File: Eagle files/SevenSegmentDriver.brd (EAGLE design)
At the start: 100 x 80 mm, 12 parts, among them IC1 74HC595D

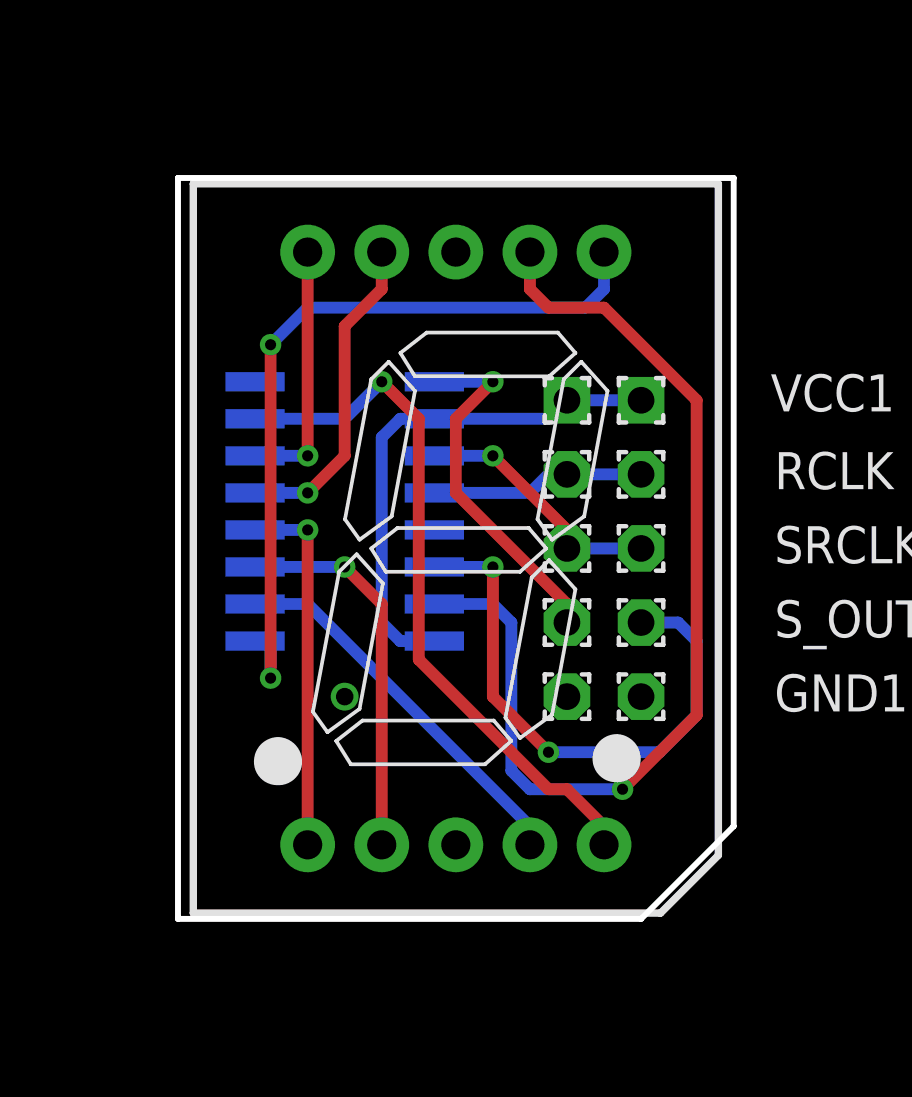
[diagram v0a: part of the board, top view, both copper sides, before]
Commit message: Ready for Fabbing
Silk Screens added and last minute DRC checks done.
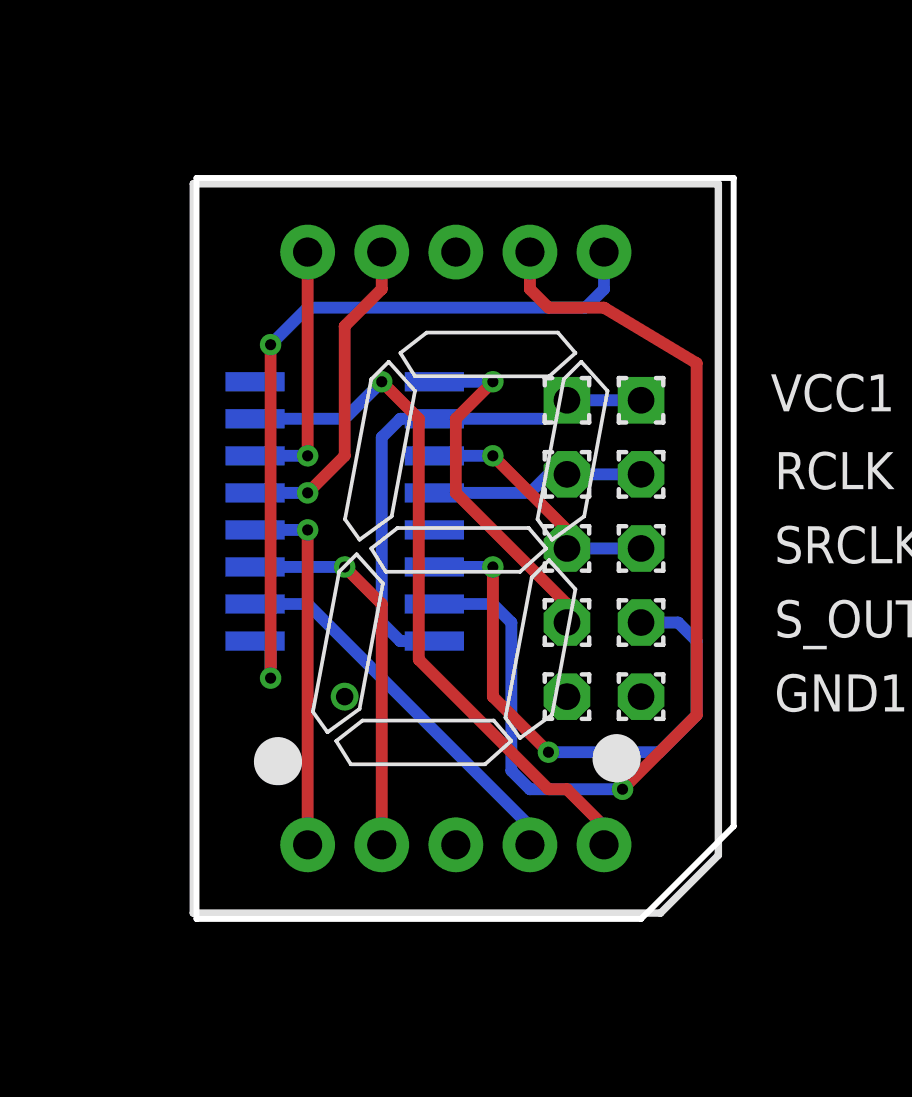
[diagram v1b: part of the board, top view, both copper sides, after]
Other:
- outline, holes or cut-outs redrawn
- board text added: "LazerTag"
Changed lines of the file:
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@@
 <layer number="24" name="bOrigins" color="15" fill="1" visible="yes" active="yes"/>
 <layer number="25" name="tNames" color="7" fill="1" visible="yes" active="yes"/>
-<layer number="26" name="bNames" color="7" fill="1" visible="yes" active="yes"/>
+<layer number="26" name="bNames" color="7" fill="1" visible="no" active="yes"/>
 <layer number="27" name="tValues" color="7" fill="1" visible="yes" active="yes"/>
 <layer number="28" name="bValues" color="7" fill="1" visible="yes" active="yes"/>
@@
 <wire x1="100" y1="80" x2="0" y2="80" width="0" layer="20"/>
 <wire x1="0" y1="80" x2="0" y2="0" width="0" layer="20"/>
-<wire x1="38.735" y1="44.45" x2="38.735" y2="19.05" width="0.2032" layer="20"/>
+<wire x1="39.37" y1="44.45" x2="39.37" y2="19.05" width="0.2032" layer="20"/>
 <wire x1="57.785" y1="22.225" x2="57.785" y2="44.45" width="0.2032" layer="20"/>
-<wire x1="57.785" y1="44.45" x2="38.735" y2="44.45" width="0.2032" layer="20"/>
-<wire x1="38.735" y1="19.05" x2="54.61" y2="19.05" width="0.2032" layer="20"/>
+<wire x1="57.785" y1="44.45" x2="39.37" y2="44.45" width="0.2032" layer="20"/>
+<wire x1="39.37" y1="19.05" x2="54.61" y2="19.05" width="0.2032" layer="20"/>
 <wire x1="54.61" y1="19.05" x2="57.785" y2="22.225" width="0.2032" layer="20"/>
-<text x="54.61" y="38.1" size="0.889" layer="24" rot="MR0">VCC</text>
-<text x="54.61" y="24.765" size="0.889" layer="24" rot="MR0">GND</text>
-<text x="50.165" y="28.575" size="0.889" layer="24" rot="MR90">SO</text>
-<text x="56.515" y="29.845" size="0.889" layer="24" rot="MR270">SI</text>
-<text x="56.515" y="32.385" size="0.889" layer="24" rot="MR270">SR</text>
-<text x="56.515" y="34.925" size="0.889" layer="24" rot="MR270">RC</text>
-<text x="45.085" y="38.1" size="0.889" layer="24" rot="MR0">IC1</text>
-<text x="42.545" y="40.005" size="0.889" layer="24" rot="MR0">G</text>
-<text x="45.085" y="40.005" size="0.889" layer="24" rot="MR0">F</text>
-<text x="52.07" y="40.005" size="0.889" layer="24" rot="MR0">A</text>
-<text x="54.61" y="40.005" size="0.889" layer="24" rot="MR0">B</text>
-<text x="44.45" y="19.685" size="0.889" layer="24" rot="MR0">E</text>
-<text x="55.88" y="21.59" size="0.889" layer="24" rot="MR0">DP</text>
-<text x="50.165" y="19.685" size="0.889" layer="24" rot="MR0">C</text>
-<text x="46.99" y="19.685" size="0.889" layer="24" rot="MR0">D</text>
-<text x="46.99" y="23.495" size="0.889" layer="24" rot="MR180">GND</text>
-<text x="48.895" y="40.64" size="0.889" layer="24" rot="MR270">GND</text>
-<text x="41.91" y="27.305" size="0.762" layer="24" rot="MR270">7 Seg Driver
+<text x="54.61" y="38.1" size="0.889" layer="22" rot="MR0">VCC</text>
+<text x="54.61" y="24.765" size="0.889" layer="22" rot="MR0">GND</text>
+<text x="50.165" y="28.575" size="0.889" layer="22" rot="MR90">SO</text>
+<text x="56.515" y="29.845" size="0.889" layer="22" rot="MR270">SI</text>
+<text x="56.515" y="32.385" size="0.889" layer="22" rot="MR270">SR</text>
+<text x="56.515" y="34.925" size="0.889" layer="22" rot="MR270">RC</text>
+<text x="45.085" y="38.1" size="0.889" layer="22" rot="MR0">IC1</text>
+<text x="42.545" y="40.005" size="0.889" layer="22" rot="MR0">G</text>
+<text x="45.085" y="40.005" size="0.889" layer="22" rot="MR0">F</text>
+<text x="52.07" y="40.005" size="0.889" layer="22" rot="MR0">A</text>
+<text x="54.61" y="40.005" size="0.889" layer="22" rot="MR0">B</text>
+<text x="44.45" y="19.685" size="0.889" layer="22" rot="MR0">E</text>
+<text x="53.34" y="19.685" size="0.889" layer="22" rot="MR0">DP</text>
+<text x="50.165" y="19.685" size="0.889" layer="22" rot="MR0">C</text>
+<text x="46.99" y="19.685" size="0.889" layer="22" rot="MR0">D</text>
+<text x="46.99" y="23.495" size="0.889" layer="22" rot="MR180">GND</text>
+<text x="48.895" y="40.64" size="0.889" layer="22" rot="MR270">GND</text>
+<text x="41.91" y="27.305" size="0.762" layer="22" rot="MR270">7 Seg Driver
 Alan F - V1.0</text>
+<text x="42.545" y="22.86" size="0.8128" layer="22" rot="MR90">LazerTag</text>
 </plain>
 <attributes>
@@
 <contactref element="IC1" pad="13"/>
 <polygon width="0.2032" layer="16">
-<vertex x="38.735" y="44.45"/>
-<vertex x="38.735" y="19.05"/>
+<vertex x="39.37" y="44.45"/>
+<vertex x="39.37" y="19.05"/>
 <vertex x="54.61" y="19.05"/>
 <vertex x="57.785" y="22.225"/>
@@
 </polygon>
 <polygon width="0.2032" layer="1">
-<vertex x="38.735" y="44.45"/>
-<vertex x="38.735" y="19.05"/>
+<vertex x="39.37" y="44.45"/>
+<vertex x="39.37" y="19.05"/>
 <vertex x="54.61" y="19.05"/>
 <vertex x="57.785" y="22.225"/>
@@
 <wire x1="53.975" y1="23.495" x2="50.8" y2="23.495" width="0.4064" layer="16"/>
 <wire x1="56.515" y1="26.035" x2="53.975" y2="23.495" width="0.4064" layer="1"/>
-<wire x1="56.515" y1="36.83" x2="56.515" y2="26.035" width="0.4064" layer="1"/>
-<wire x1="53.34" y1="40.005" x2="56.515" y2="36.83" width="0.4064" layer="1"/>
+<wire x1="56.515" y1="38.1" x2="56.515" y2="26.035" width="0.4064" layer="1"/>
+<wire x1="53.34" y1="40.005" x2="56.515" y2="38.1" width="0.4064" layer="1"/>
 <wire x1="51.435" y1="40.005" x2="53.34" y2="40.005" width="0.4064" layer="1"/>
 <via x="53.975" y="23.495" extent="1-16" drill="0.381"/>

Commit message: Fixes
Removed outer footprint of board so that each board is now the correct
size instead of that of the default footprint.
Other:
- board size 100 x 80 mm -> 18.4 x 25.4 mm
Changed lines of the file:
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@@
 <board>
 <plain>
-<wire x1="0" y1="0" x2="100" y2="0" width="0" layer="20"/>
-<wire x1="100" y1="0" x2="100" y2="80" width="0" layer="20"/>
-<wire x1="100" y1="80" x2="0" y2="80" width="0" layer="20"/>
-<wire x1="0" y1="80" x2="0" y2="0" width="0" layer="20"/>
 <wire x1="39.37" y1="44.45" x2="39.37" y2="19.05" width="0.2032" layer="20"/>
 <wire x1="57.785" y1="22.225" x2="57.785" y2="44.45" width="0.2032" layer="20"/>

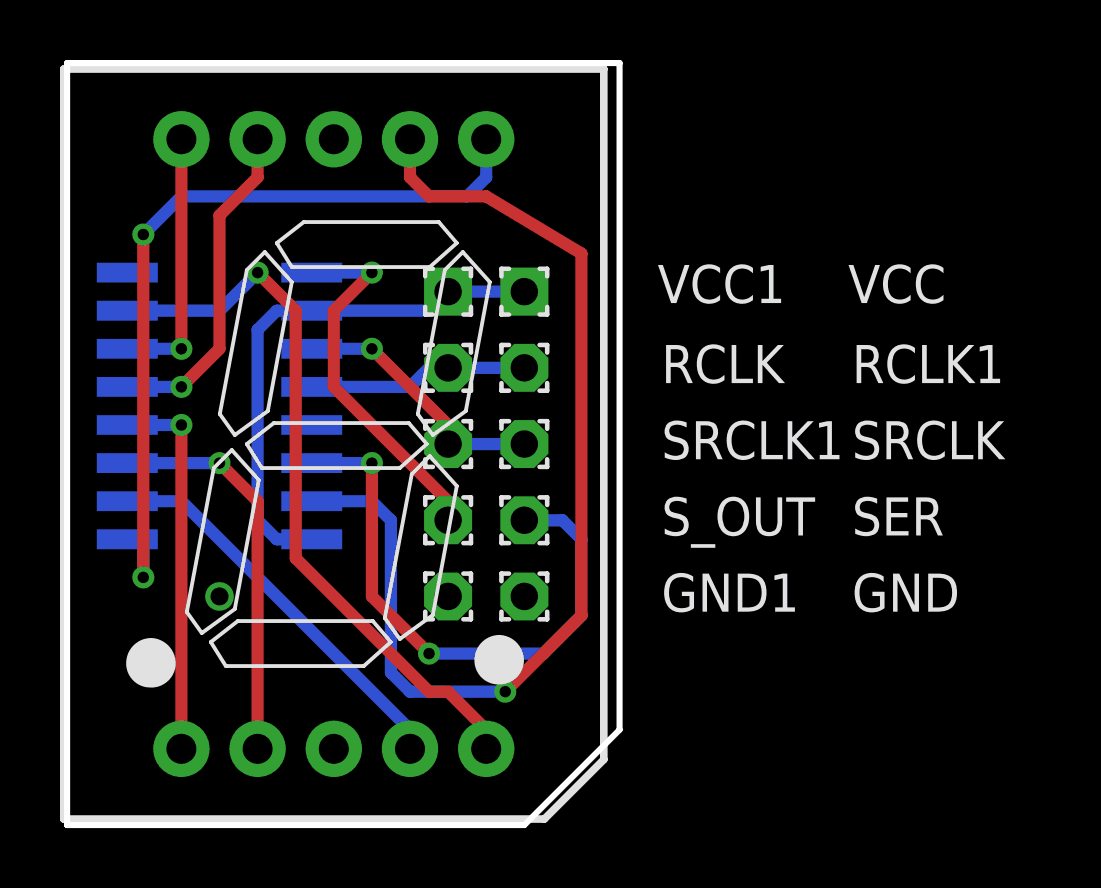
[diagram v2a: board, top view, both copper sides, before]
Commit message: aaaaaaaaaaaaaaaaaaaaaaaaaaaaaaaaaaaa
Cleaned up schematics, replaced wire solder points with header pin
mounts for standardization, recreated a broken file and dealt with the
confusion and insanity that followed.
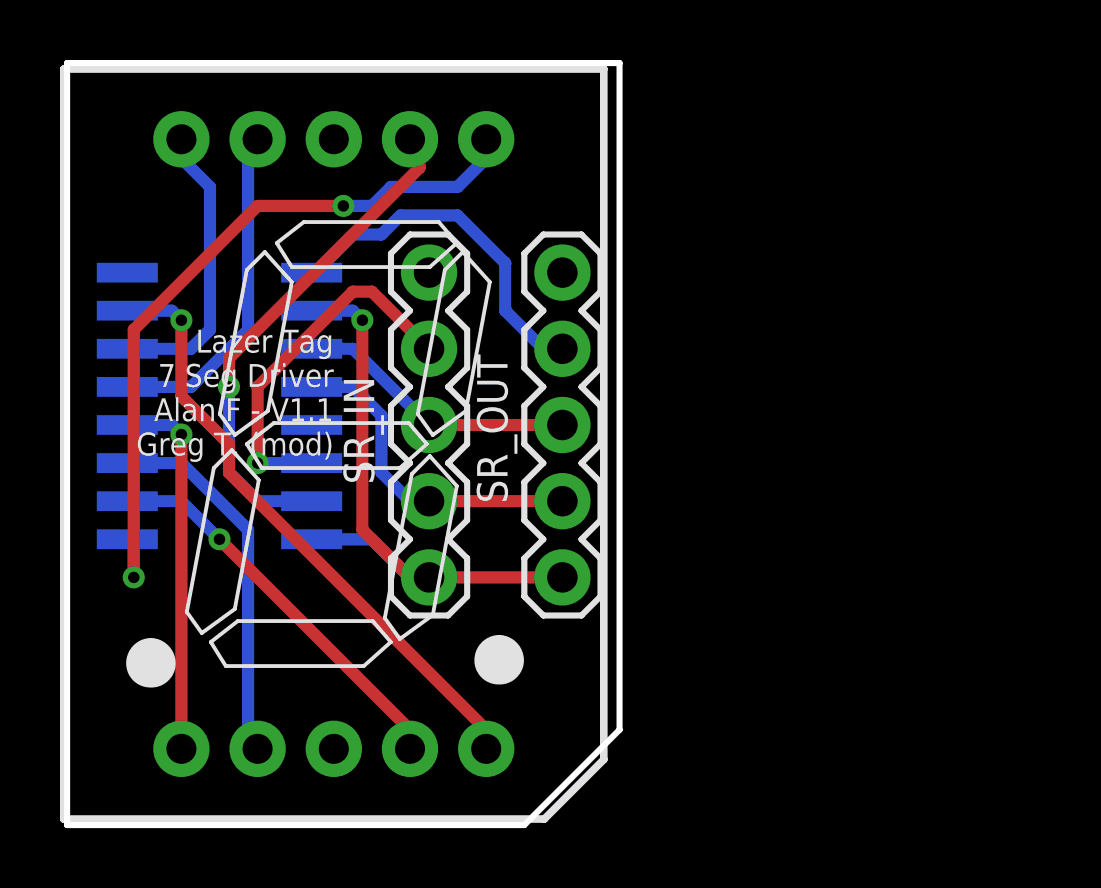
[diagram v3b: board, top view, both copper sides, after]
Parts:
- removed GND, GND1, RCLK, RCLK1, SER, SRCLK, SRCLK1, S_OUT: WIREPAD1,6/0,9, wirepad:1,6/0,9
- removed VCC, VCC1: WIREPAD1,6/0,9, smallestWirepadSquare:1,6/0,9
- added SR_IN, SR_OUT: (no value), SparkFun-Connectors:1X05
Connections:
- removed net N$11: IC1.9, S_OUT.1
- removed net N$12: IC1.12, RCLK.1, RCLK1.1
- removed net N$13: IC1.11, SRCLK.1, SRCLK1.1
- removed net N$14: IC1.SER, SER.1
- new net RCLK: IC1.12, SR_IN.2, SR_OUT.2
- new net SCLK: IC1.11, SR_IN.3, SR_OUT.3
- new net SER_IN: IC1.SER, SR_IN.4
- new net SER_OUT: IC1.9, SR_OUT.4
- net GND: now also SR_IN.5, SR_OUT.5; no longer GND.1, GND1.1
- net VCC: now also SR_IN.1, SR_OUT.1; no longer VCC.1, VCC1.1
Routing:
- net N$14: track 19.5 -> 0.00 mm, vias 2 -> 0
- net N$3: track 35.5 -> 17.0 mm
- net N$11: track 12.4 -> 0.00 mm, vias 1 -> 0
- net SER_IN: track 0.00 -> 12.2 mm, vias 0 -> 1
- net SER_OUT: track 0.00 -> 11.9 mm
- net RCLK: track 0.00 -> 11.1 mm
- net SCLK: track 0.00 -> 9.41 mm
- net N$13: track 8.77 -> 0.00 mm, vias 1 -> 0
- net N$12: track 7.35 -> 0.00 mm
- net N$10: track 24.3 -> 20.4 mm
- net VCC: track 17.8 -> 20.6 mm, vias 0 -> 1
- net N$4: track 26.7 -> 24.5 mm
- net N$9: track 8.79 -> 9.76 mm, vias 1 -> 0
- net N$6: track 13.1 -> 12.4 mm, vias 1 -> 0
- net N$8: track 11.1 -> 11.3 mm, vias 1 -> 0
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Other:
- board text added: "Lazer Tag 7 Seg Driver Alan F - V1.1 Greg T. (mod)"
- board text removed: "7 Seg Driver Alan F - V1.0"
- board text removed: "LazerTag"

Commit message: Fixes
more fixes >:|
should e ready for fabbing
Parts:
- moved SR_IN 10.2 mm to (51.4, 37.5), turned to 270 degrees
- moved SR_OUT 10.2 mm to (55.9, 37.5), turned to 270 degrees
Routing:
- net SER_OUT: track 11.9 -> 23.2 mm, vias 0 -> 1
- net SER_IN: track 12.2 -> 4.44 mm, vias 1 -> 0
- net VCC: track 20.6 -> 27.9 mm, vias 1 -> 2
- net N$8: track 11.3 -> 14.1 mm
- net N$4: track 24.5 -> 22.8 mm
- net RCLK: track 11.1 -> 9.41 mm
- net N$3: track 17.0 -> 15.7 mm
- net SCLK: track 9.41 -> 10.7 mm, vias 0 -> 1
- net N$7: track 12.4 -> 13.6 mm, vias 1 -> 0
- net N$9: track 9.76 -> 8.79 mm, vias 0 -> 1
- net N$6: track 12.4 -> 11.8 mm, vias 0 -> 1
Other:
- board text removed: "RC"
- board text removed: "SI"
- board text removed: "SO"
- board text removed: "SR"
